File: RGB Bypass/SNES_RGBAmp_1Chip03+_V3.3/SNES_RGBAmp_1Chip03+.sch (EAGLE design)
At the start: 30 parts

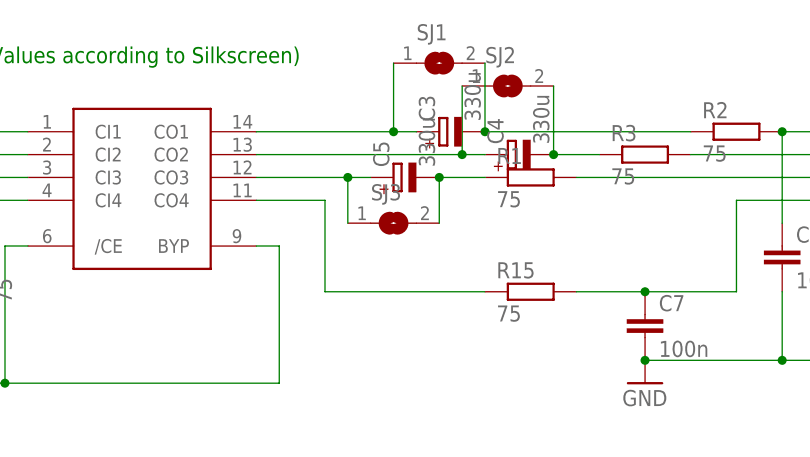
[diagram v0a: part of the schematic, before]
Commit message: Update: 330uF tantalum in CSYNC line at the output of the THS7374.
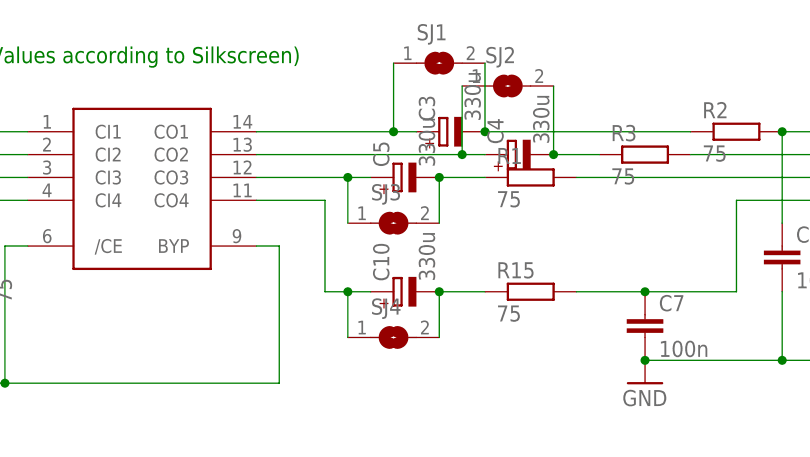
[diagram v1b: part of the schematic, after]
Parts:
- added C10: 330u, rcl:CPOL-EUSMCD
- added SJ4: (no value), jumper:SJ
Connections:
- new net N$19: C10.-, R15.1, SJ4.2
- net N$18: now also C10.+, SJ4.1; no longer R15.1
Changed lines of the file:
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@@
 <?xml version="1.0" encoding="utf-8"?>
 <!DOCTYPE eagle SYSTEM "eagle.dtd">
-<eagle version="6.4">
+<eagle version="7.5.0">
 <drawing>
 <settings>
@@
 <part name="C8" library="snescart" deviceset="C0805" device="" value="100n"/>
 <part name="C9" library="snescart" deviceset="C0805" device="" value="100n"/>
+<part name="C10" library="rcl" deviceset="CPOL-EU" device="SMCD" value="330u"/>
+<part name="SJ4" library="jumper" deviceset="SJ" device=""/>
 </parts>
 <sheets>
@@
 <instance part="C8" gate="G$1" x="83.82" y="-12.7"/>
 <instance part="C9" gate="G$1" x="91.44" y="-12.7"/>
+<instance part="C10" gate="G$1" x="33.02" y="-17.78" rot="R90"/>
+<instance part="SJ4" gate="1" x="33.02" y="-22.86"/>
 </instances>
 <busses>
@@
 <net name="N$18" class="0">
 <segment>
-<pinref part="R15" gate="G$1" pin="1"/>
 <pinref part="U$2" gate="G$1" pin="CO4"/>
 <wire x1="17.78" y1="-7.62" x2="25.4" y2="-7.62" width="0.1524" layer="91"/>
 <wire x1="25.4" y1="-7.62" x2="25.4" y2="-17.78" width="0.1524" layer="91"/>
-<wire x1="43.18" y1="-17.78" x2="25.4" y2="-17.78" width="0.1524" layer="91"/>
-</segment>
-</net>
+<pinref part="C10" gate="G$1" pin="+"/>
+<wire x1="30.48" y1="-17.78" x2="27.94" y2="-17.78" width="0.1524" layer="91"/>
+<pinref part="SJ4" gate="1" pin="1"/>
+<wire x1="27.94" y1="-17.78" x2="25.4" y2="-17.78" width="0.1524" layer="91"/>
+<wire x1="27.94" y1="-22.86" x2="27.94" y2="-17.78" width="0.1524" layer="91"/>
+<junction x="27.94" y="-17.78"/>
+</segment>
+</net>
+<net name="N$19" class="0">
+<segment>
+<pinref part="R15" gate="G$1" pin="1"/>
+<wire x1="43.18" y1="-17.78" x2="38.1" y2="-17.78" width="0.1524" layer="91"/>
+<pinref part="C10" gate="G$1" pin="-"/>
+<pinref part="SJ4" gate="1" pin="2"/>
+<wire x1="38.1" y1="-22.86" x2="38.1" y2="-17.78" width="0.1524" layer="91"/>
+<junction x="38.1" y="-17.78"/>
+</segment>
+</net>

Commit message: Update silkscreen
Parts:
- removed R13, R14, R15: 75, snescart:R0805
- added R7: 9.53k, snescart:R0805
- added R8, R9: 8.45k, snescart:R0805
- C10: value 330u -> 47p; device rcl:CPOL-EUSMCD -> snescart:C0805
- C6: value 100n -> 330u; device snescart:C0805 -> rcl:CPOL-EUSMCD
- C7, C8, C9: value 100n -> 47p
- R10: value 75 -> 75-421
- R11: value 75 -> 5.0k
- R12: value 75 -> 4.3k
- R4: value 75 -> 806
- R5, R6: value 75 -> 1.3k
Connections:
- removed net N$3: R12.1, R4.2, U$2G$1.CI3
- new net R9: R6.1, R9.2, U$2G$1.CI3
- net GND: now also C10.2, R12.1, R7.1, R8.1, R9.1; no longer C6.2, R14.1, R4.1, R5.1, R6.1
- net N$1: now also R4.1, R7.2; no longer R10.1, R6.2
- net N$10: now also R11.1, R12.2; no longer R13.1, R14.2
- net N$13: now also R2.1; no longer R3.1
- net N$14: now also R4.2; no longer R10.2
- net N$15: now also R5.2; no longer R11.2
- net N$16: now also R6.2; no longer R12.2
- net N$17: now also R11.2; no longer R13.2
- net N$18: now also C6.+; no longer C10.+
- net N$19: now also C6.-, R10.1; no longer C10.-, R15.1
- net N$2: now also R5.1, R8.2; no longer R11.1, R5.2
- net N$20: now also C10.1, R10.2; no longer C7.1, R15.2
- net N$4: now also R1.1; no longer R2.1
- net N$5: now also C7.1, R1.2; no longer C6.1, R2.2
- net N$6: now also R2.2; no longer R3.2
- net N$8: now also R3.1; no longer R1.1
- net N$9: now also R3.2; no longer R1.2
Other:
- note removed: "(Values according to Silkscreen)"
- moved on the sheet: C7, R1, R10, R11, R12, R2, R3, R4, R5, R6
